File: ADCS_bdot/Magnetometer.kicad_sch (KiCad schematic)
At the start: 1 part, among them IC2 IIS2MDCTR

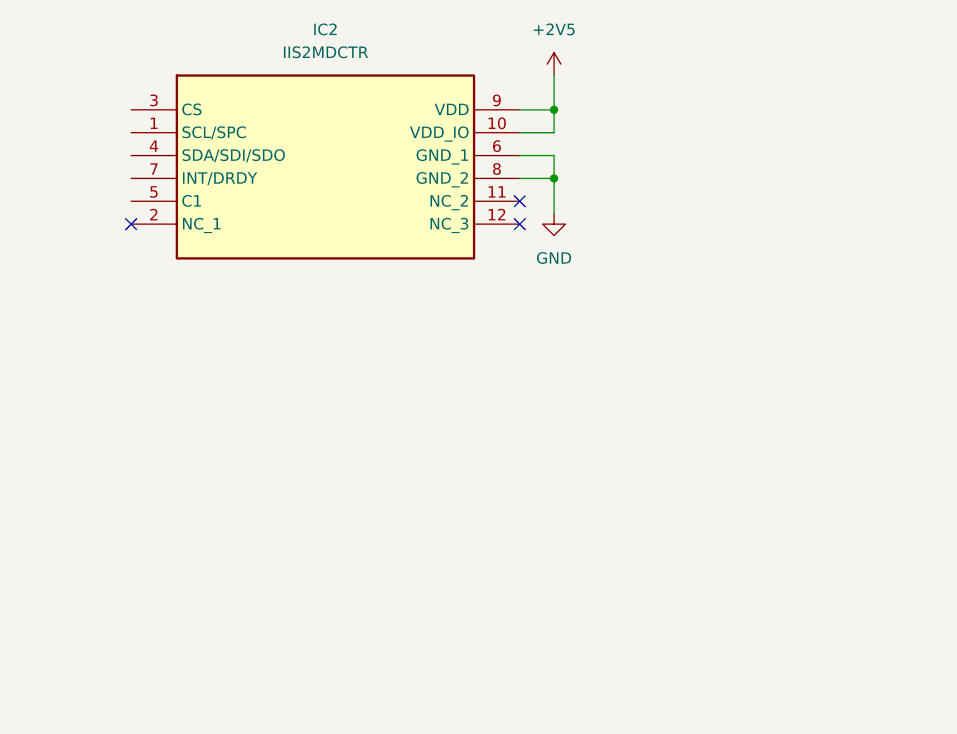
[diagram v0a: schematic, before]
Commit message: feat: Gyro and Mag RC Filter
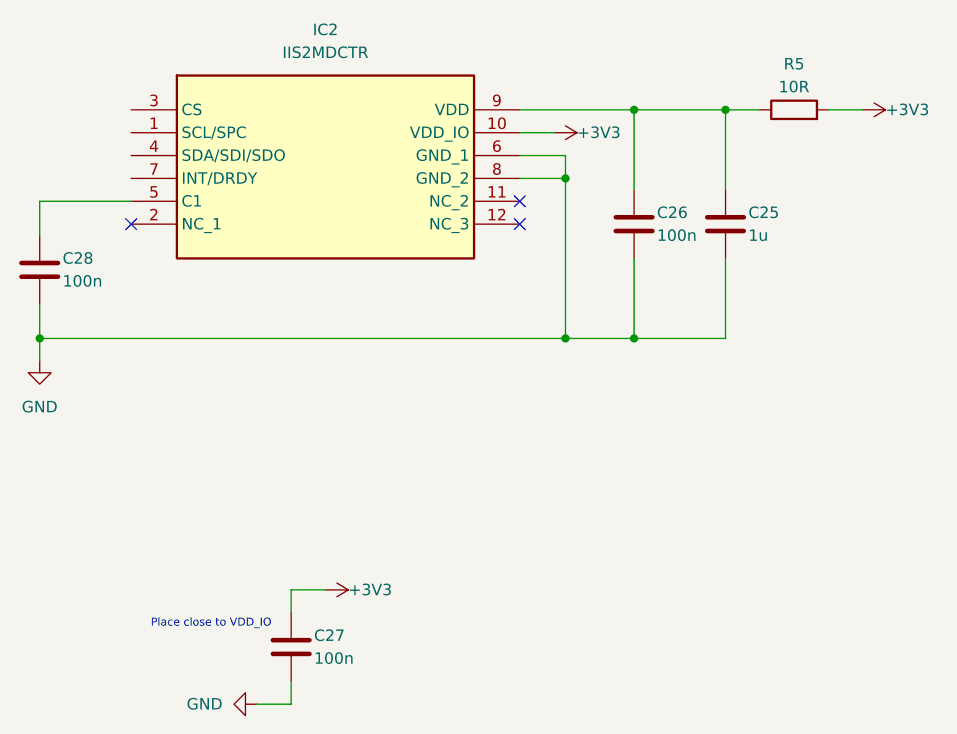
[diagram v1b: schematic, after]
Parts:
- added C25: 1u, symbol Device:C
- added C26, C27, C28: 100n, symbol Device:C
- added R5: 10R, symbol Device:R
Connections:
- net GND: now also C25.2, C26.2, C27.2, C28.2
- net at IC2.5 (C1): now also C28.1
- net +2V5: no longer names the net of IC2.9 (VDD)
- net +2V5: now also C25.1, C26.1, R5.1; no longer IC2.10 (VDD_IO)
- new net +3V3: C27.1, IC2.10 (VDD_IO), R5.2
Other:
- note added: "Place close to VDD_IO"
